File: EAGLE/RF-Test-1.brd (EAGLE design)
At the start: 20.3 x 35.6 mm, 9 parts, among them X1 SMA-142-0701-851/861, X2 IPEX-20279-001E

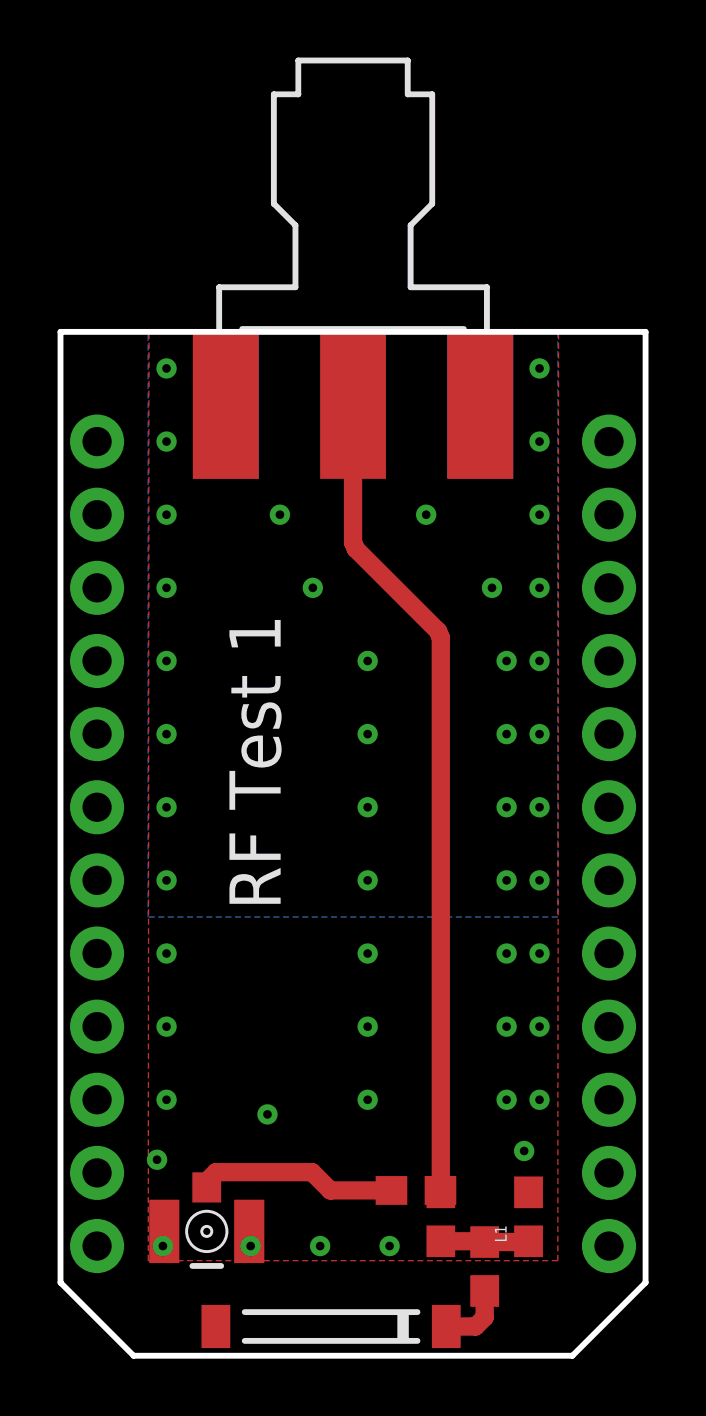
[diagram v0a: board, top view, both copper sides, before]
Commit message: Minor twak of SMA position. Remove thermals on bottom layer.
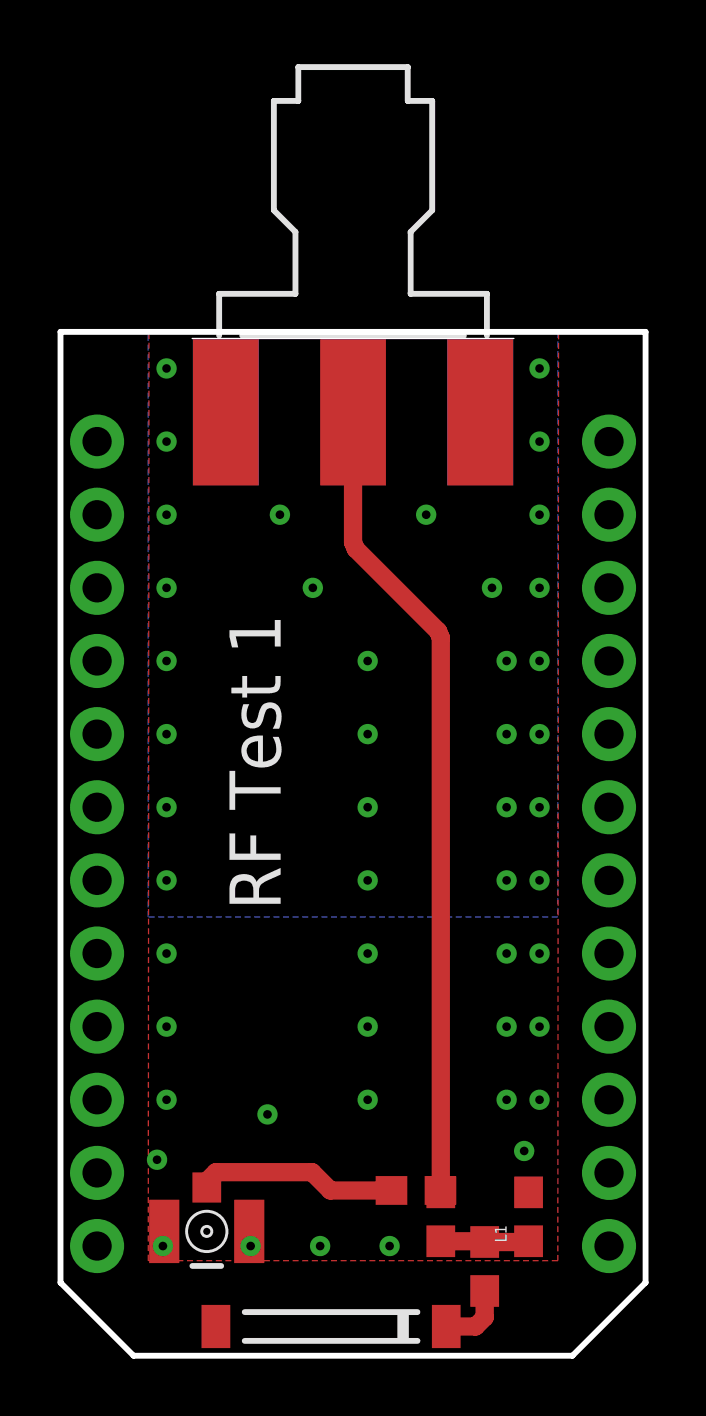
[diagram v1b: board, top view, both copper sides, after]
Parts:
- moved X1 0.23 mm to (10.2, 32.8)
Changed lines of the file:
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@@
 <layer number="19" name="Unrouted" color="6" fill="1" visible="yes" active="yes"/>
 <layer number="20" name="Dimension" color="6" fill="1" visible="yes" active="yes"/>
-<layer number="21" name="tPlace" color="16" fill="1" visible="yes" active="yes"/>
-<layer number="22" name="bPlace" color="14" fill="1" visible="yes" active="yes"/>
+<layer number="21" name="tPlace" color="16" fill="1" visible="no" active="yes"/>
+<layer number="22" name="bPlace" color="14" fill="1" visible="no" active="yes"/>
 <layer number="23" name="tOrigins" color="15" fill="1" visible="yes" active="yes"/>
 <layer number="24" name="bOrigins" color="15" fill="1" visible="yes" active="yes"/>
@@
 <layer number="27" name="tValues" color="7" fill="1" visible="no" active="yes"/>
 <layer number="28" name="bValues" color="7" fill="1" visible="no" active="yes"/>
-<layer number="29" name="tStop" color="7" fill="3" visible="yes" active="yes"/>
+<layer number="29" name="tStop" color="7" fill="3" visible="no" active="yes"/>
 <layer number="30" name="bStop" color="7" fill="6" visible="no" active="yes"/>
 <layer number="31" name="tCream" color="7" fill="4" visible="yes" active="yes"/>
@@
 <layer number="49" name="Reference" color="7" fill="1" visible="no" active="yes"/>
 <layer number="50" name="dxf" color="7" fill="1" visible="no" active="yes"/>
-<layer number="51" name="tDocu" color="6" fill="1" visible="yes" active="yes"/>
+<layer number="51" name="tDocu" color="6" fill="1" visible="no" active="yes"/>
 <layer number="52" name="bDocu" color="7" fill="1" visible="no" active="yes"/>
 <layer number="53" name="tGND_GNDA" color="7" fill="9" visible="no" active="no"/>
@@
 <attribute name="VALUE" x="15.113" y="1.651" size="1.27" layer="27" rot="R90"/>
 </element>
-<element name="X1" library="con-coax" package="J502-ND-142-0701-851/861" value="SMA-142-0701-851/861" x="10.16" y="33.02" smashed="yes" rot="R270">
-<attribute name="OC_NEWARK" value="99F6798" x="10.16" y="33.02" size="1.778" layer="27" rot="R270" display="off"/>
-<attribute name="MPN" value="142-0701-851" x="10.16" y="33.02" size="1.778" layer="27" rot="R270" display="off"/>
-<attribute name="MF" value="JOHNSON COMPONENTS" x="10.16" y="33.02" size="1.778" layer="27" rot="R270" display="off"/>
-<attribute name="OC_FARNELL" value="1019325" x="10.16" y="33.02" size="1.778" layer="27" rot="R270" display="off"/>
-<attribute name="VALUE" x="1.27" y="31.75" size="1.778" layer="27" rot="R270"/>
+<element name="X1" library="con-coax" package="J502-ND-142-0701-851/861" value="SMA-142-0701-851/861" x="10.16" y="32.7914" smashed="yes" rot="R270">
+<attribute name="OC_NEWARK" value="99F6798" x="10.16" y="32.7914" size="1.778" layer="27" rot="R270" display="off"/>
+<attribute name="MPN" value="142-0701-851" x="10.16" y="32.7914" size="1.778" layer="27" rot="R270" display="off"/>
+<attribute name="MF" value="JOHNSON COMPONENTS" x="10.16" y="32.7914" size="1.778" layer="27" rot="R270" display="off"/>
+<attribute name="OC_FARNELL" value="1019325" x="10.16" y="32.7914" size="1.778" layer="27" rot="R270" display="off"/>
+<attribute name="VALUE" x="1.27" y="31.5214" size="1.778" layer="27" rot="R270"/>
 </element>
 </elements>
@@
 <contactref element="X1" pad="G@3"/>
 <contactref element="X1" pad="G@2"/>
-<polygon width="0.1524" layer="16">
+<polygon width="0.1524" layer="16" thermals="no">
 <vertex x="3.048" y="33.02"/>
 <vertex x="17.272" y="33.02"/>
@@
 <wire x1="13.11500625" y1="22.62279375" x2="10.25299375" y2="25.48480625" width="0.635" layer="1"/>
 <wire x1="10.25299375" y1="25.48480625" x2="10.16" y2="25.7093125" width="0.635" layer="1"/>
-<wire x1="10.16" y1="25.7093125" x2="10.16" y2="30.4546" width="0.635" layer="1"/>
+<wire x1="10.16" y1="25.7093125" x2="10.16" y2="30.226" width="0.635" layer="1"/>
 <wire x1="13.208" y1="3.136" x2="13.1944" y2="3.2004" width="0" layer="19" extent="1-1"/>
 </signal>
